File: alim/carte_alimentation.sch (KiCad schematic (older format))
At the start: 26 parts, among them J11 Conn_01x02_Male, J12 Conn_01x02_Male, J21 Conn_01x02_Male, J22 Conn_01x02_Male, J31 Conn_01x02_Male, J32 Conn_01x02_Male, J40 Conn_01x02_Male, J41 Conn_01x02_Male, J42 Conn_01x02_Male, J43 Conn_01x02_Male, U1 LM2576T-5, U2 LM2576T-5, U3 LM2576T-5

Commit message: ajout relais arret urgence
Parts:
- added K4: DIPxx-1Axx-11x, Relay_THT:Relay_StandexMeder_DIP_LowProfile, symbol Relay:DIPxx-1Axx-11x
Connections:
- wire segments 69 -> 72
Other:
- note added: "arret urgence NC\n"
- note removed: "arret urgence\n"
- moved on the sheet: C11, C12, C21, C22, D1, D2, J11, J12, J21, J22, J41, J42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

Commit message: Retrait relais, on fait passer toute la puissance par les arrêt d'urgence
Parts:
- removed K4: DIPxx-1Axx-11x, Relay_THT:Relay_StandexMeder_DIP_LowProfile, symbol Relay:DIPxx-1Axx-11x
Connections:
- wire segments 72 -> 69
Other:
- moved on the sheet: J42
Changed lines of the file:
@@
 	1    0    0    -1
 $EndComp
-Text Notes 3100 1200 0    50   ~ 0
+Text Notes 2950 1700 0    50   ~ 0
 arret urgence NC\n
 Wire Wire Line
@@
 	8200 3950 9050 3950
 $Comp
-L Relay:DIPxx-1Axx-11x K4
-U 1 1 5DE5847D
-P 2850 1800
-F 0 "K4" V 2283 1800 50  0000 C CNN
-F 1 "DIPxx-1Axx-11x" V 2374 1800 50  0000 C CNN
-F 2 "Relay_THT:Relay_StandexMeder_DIP_LowProfile" H 3200 1750 50  0001 L CNN
-F 3 "https://standexelectronics.com/wp-content/uploads/datasheet_reed_relay_DIP.pdf" H 2850 1800 50  0001 C CNN
-	1    2850 1800
-	0    1    1    0
-$EndComp
-Wire Wire Line
-	2550 2000 2450 2000
-$Comp
 L Connector:Conn_01x02_Male J42
 U 1 1 5DE1629E
-P 3250 1400
-F 0 "J42" V 3312 1444 50  0000 L CNN
-F 1 "Conn_01x02_Male" V 3403 1444 50  0000 L CNN
-F 2 "TerminalBlock:TerminalBlock_bornier-2_P5.08mm" H 3250 1400 50  0001 C CNN
-F 3 "~" H 3250 1400 50  0001 C CNN
-	1    3250 1400
+P 3150 1800
+F 0 "J42" V 3212 1844 50  0000 L CNN
+F 1 "Conn_01x02_Male" V 3303 1844 50  0000 L CNN
+F 2 "TerminalBlock:TerminalBlock_bornier-2_P5.08mm" H 3150 1800 50  0001 C CNN
+F 3 "~" H 3150 1800 50  0001 C CNN
+	1    3150 1800
 	0    1    1    0
 $EndComp
@@
 Wire Wire Line
 	4700 2000 3150 2000
-$Comp
-L power:GND #PWR0124
-U 1 1 5DE8EA76
-P 3250 1600
-F 0 "#PWR0124" H 3250 1350 50  0001 C CNN
-F 1 "GND" H 3255 1427 50  0000 C CNN
-F 2 "" H 3250 1600 50  0001 C CNN
-F 3 "" H 3250 1600 50  0001 C CNN
-	1    3250 1600
-	1    0    0    -1
-$EndComp
-Wire Wire Line
-	2550 1600 1950 1600
-Wire Wire Line
-	1950 1600 1950 2000
-Wire Wire Line
-	1900 2000 1950 2000
-Wire Wire Line
-	1950 2000 2150 2000
-Connection ~ 1950 2000
 Text Notes 4600 1150 0    50   ~ 0
 puissance moteurs\n
+Wire Wire Line
+	1900 2000 2150 2000
+Wire Wire Line
+	2450 2000 3050 2000
 $EndSCHEMATC

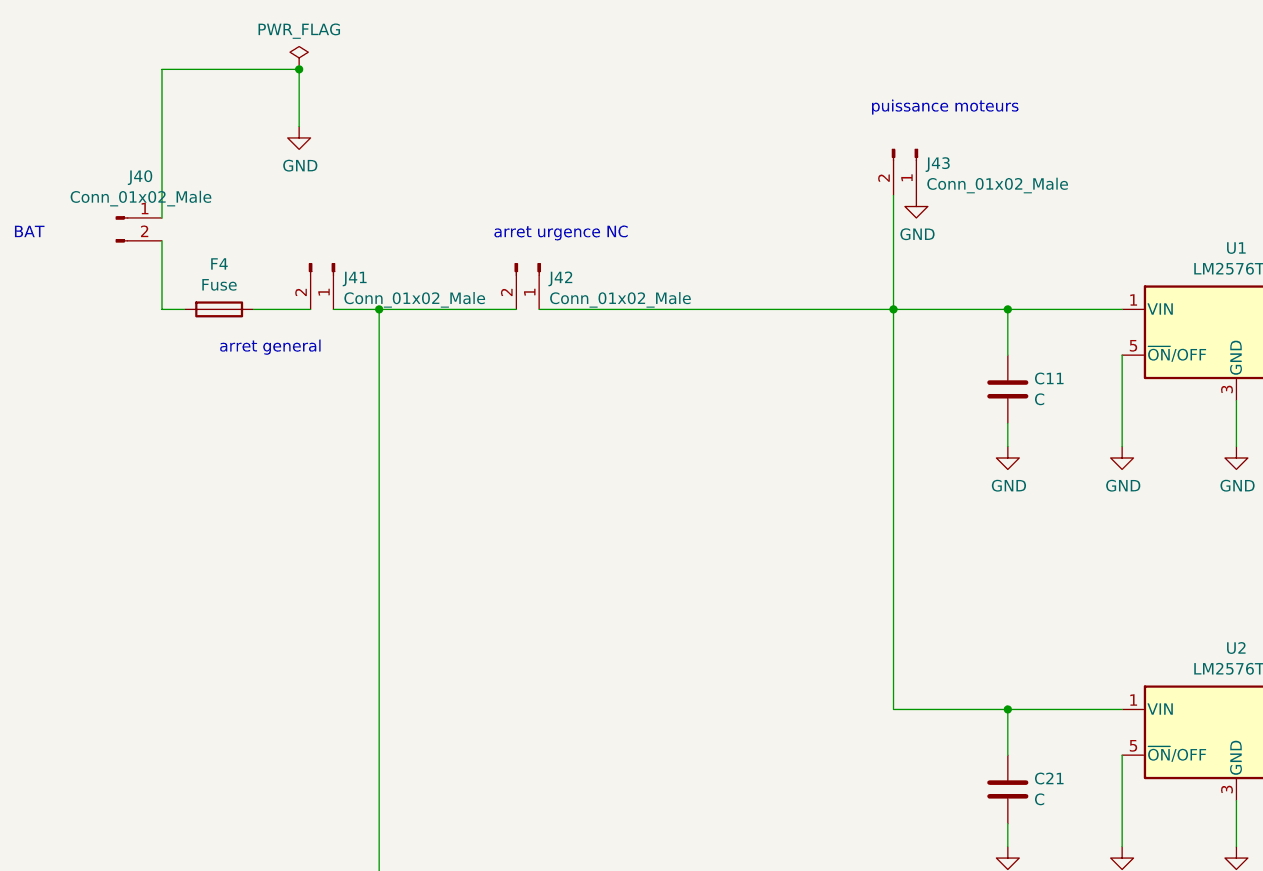
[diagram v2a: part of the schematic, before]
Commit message: ajout deuxieme fusible et empreinte
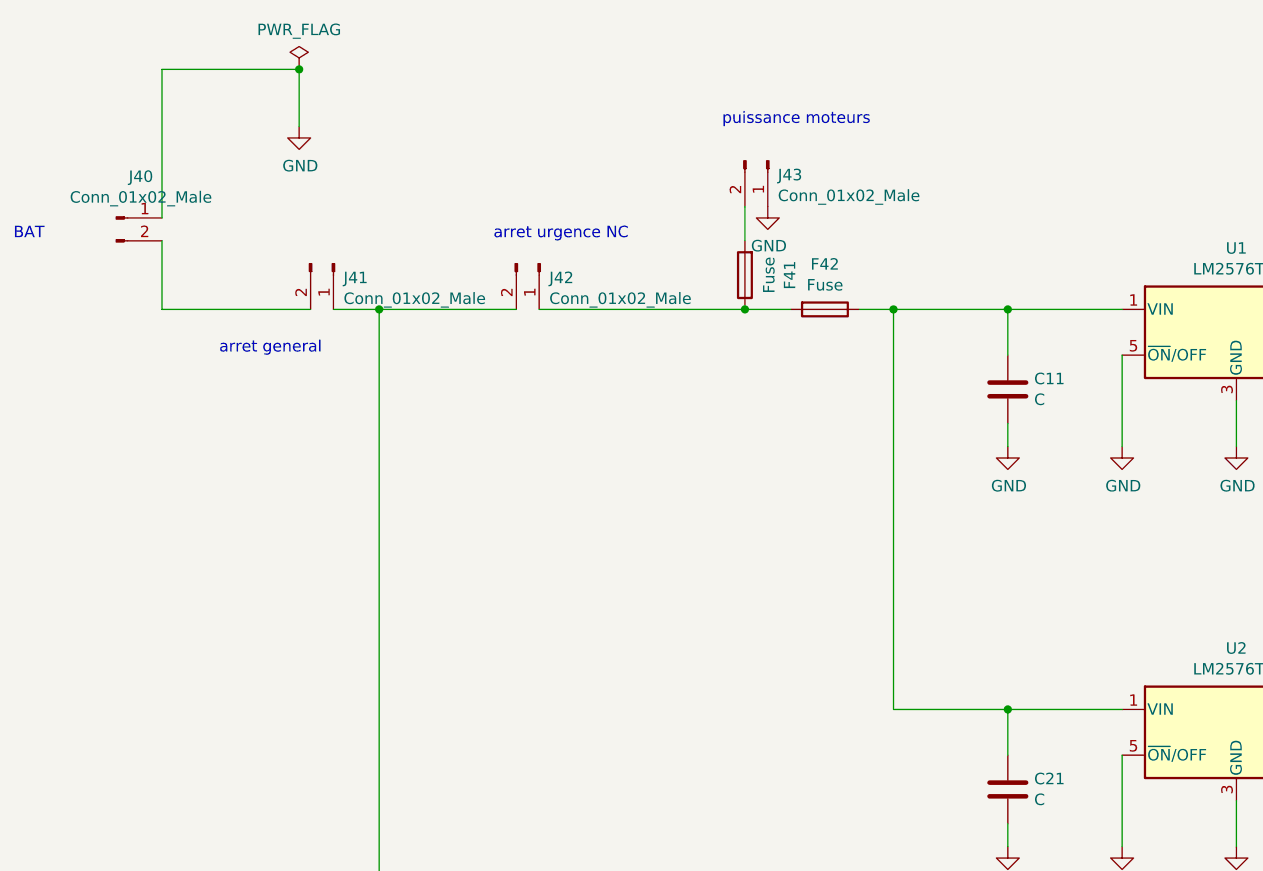
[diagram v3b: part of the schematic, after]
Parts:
- added F42: Fuse, symbol Device:Fuse
- C11, C12, C21, C22, C31, C32: footprint (none) -> Capacitor_THT:CP_Radial_D10.0mm_P5.00mm
- D1, D2, D3: footprint (none) -> Diode_THT:D_DO-27_P12.70mm_Horizontal
- renumbered F4 to F41
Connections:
- net at C11.1, C21.1, U1.1 (VIN)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: now also F42.1; no longer J42.1 (Pin_1), J43.2 (Pin_2)
- net at J40.2 (Pin_2): now also J41.2 (Pin_2); no longer F41.2
- net at F41.1: now also J42.1 (Pin_1), F42.2; no longer J41.2 (Pin_2)
- new net: F41.2, J43.2 (Pin_2)
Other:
- moved on the sheet: F41, J43
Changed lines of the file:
@@
 F 0 "C22" H 8085 4054 50  0000 R CNN
 F 1 "C" H 8085 4145 50  0000 R CNN
-F 2 "" H 8238 3950 50  0001 C CNN
+F 2 "Capacitor_THT:CP_Radial_D10.0mm_P5.00mm" H 8238 3950 50  0001 C CNN
 F 3 "~" H 8200 4100 50  0001 C CNN
 	1    8200 4100
@@
 F 0 "D2" V 7154 4179 50  0000 L CNN
 F 1 "D_Schottky" V 7245 4179 50  0000 L CNN
-F 2 "" H 7200 4100 50  0001 C CNN
+F 2 "Diode_THT:D_DO-27_P12.70mm_Horizontal" H 7200 4100 50  0001 C CNN
 F 3 "~" H 7200 4100 50  0001 C CNN
 	1    7200 4100
@@
 F 0 "C21" H 5315 4146 50  0000 L CNN
 F 1 "C" H 5315 4055 50  0000 L CNN
-F 2 "" H 5238 3950 50  0001 C CNN
+F 2 "Capacitor_THT:CP_Radial_D10.0mm_P5.00mm" H 5238 3950 50  0001 C CNN
 F 3 "~" H 5200 4100 50  0001 C CNN
 	1    5200 4100
@@
 F 0 "C12" H 8085 2304 50  0000 R CNN
 F 1 "C" H 8085 2395 50  0000 R CNN
-F 2 "" H 8238 2200 50  0001 C CNN
+F 2 "Capacitor_THT:CP_Radial_D10.0mm_P5.00mm" H 8238 2200 50  0001 C CNN
 F 3 "~" H 8200 2350 50  0001 C CNN
 	1    8200 2350
@@
 F 0 "D1" V 7154 2429 50  0000 L CNN
 F 1 "D_Schottky" V 7245 2429 50  0000 L CNN
-F 2 "" H 7200 2350 50  0001 C CNN
+F 2 "Diode_THT:D_DO-27_P12.70mm_Horizontal" H 7200 2350 50  0001 C CNN
 F 3 "~" H 7200 2350 50  0001 C CNN
 	1    7200 2350
@@
 F 0 "C11" H 5315 2396 50  0000 L CNN
 F 1 "C" H 5315 2305 50  0000 L CNN
-F 2 "" H 5238 2200 50  0001 C CNN
+F 2 "Capacitor_THT:CP_Radial_D10.0mm_P5.00mm" H 5238 2200 50  0001 C CNN
 F 3 "~" H 5200 2350 50  0001 C CNN
 	1    5200 2350
@@
 F 0 "C32" H 7385 5804 50  0000 R CNN
 F 1 "C" H 7385 5895 50  0000 R CNN
-F 2 "" H 7538 5700 50  0001 C CNN
+F 2 "Capacitor_THT:CP_Radial_D10.0mm_P5.00mm" H 7538 5700 50  0001 C CNN
 F 3 "~" H 7500 5850 50  0001 C CNN
 	1    7500 5850
@@
 F 0 "D3" V 6454 5929 50  0000 L CNN
 F 1 "D_Schottky" V 6545 5929 50  0000 L CNN
-F 2 "" H 6500 5850 50  0001 C CNN
+F 2 "Diode_THT:D_DO-27_P12.70mm_Horizontal" H 6500 5850 50  0001 C CNN
 F 3 "~" H 6500 5850 50  0001 C CNN
 	1    6500 5850
@@
 F 0 "C31" H 4615 5896 50  0000 L CNN
 F 1 "C" H 4615 5805 50  0000 L CNN
-F 2 "" H 4538 5700 50  0001 C CNN
+F 2 "Capacitor_THT:CP_Radial_D10.0mm_P5.00mm" H 4538 5700 50  0001 C CNN
 F 3 "~" H 4500 5850 50  0001 C CNN
 	1    4500 5850
@@
 arret urgence NC\n
 Wire Wire Line
-	4700 2000 4700 3750
-Connection ~ 4700 2000
-Wire Wire Line
-	4700 2000 5200 2000
-Wire Wire Line
 	1500 2000 1500 1700
 Wire Wire Line
@@
 L Connector:Conn_01x02_Male J43
 U 1 1 5DE73A34
-P 4800 1300
-F 0 "J43" V 4862 1344 50  0000 L CNN
-F 1 "Conn_01x02_Male" V 4953 1344 50  0000 L CNN
-F 2 "TerminalBlock:TerminalBlock_bornier-2_P5.08mm" H 4800 1300 50  0001 C CNN
-F 3 "~" H 4800 1300 50  0001 C CNN
-	1    4800 1300
-	0    1    1    0
-$EndComp
-Wire Wire Line
-	4700 2000 4700 1500
+P 4150 1350
+F 0 "J43" V 4212 1394 50  0000 L CNN
+F 1 "Conn_01x02_Male" V 4303 1394 50  0000 L CNN
+F 2 "TerminalBlock:TerminalBlock_bornier-2_P5.08mm" H 4150 1350 50  0001 C CNN
+F 3 "~" H 4150 1350 50  0001 C CNN
+	1    4150 1350
+	0    1    1    0
+$EndComp
 $Comp
 L power:GND #PWR0118
 U 1 1 5DE759C9
-P 4800 1500
-F 0 "#PWR0118" H 4800 1250 50  0001 C CNN
-F 1 "GND" H 4805 1327 50  0000 C CNN
-F 2 "" H 4800 1500 50  0001 C CNN
-F 3 "" H 4800 1500 50  0001 C CNN
-	1    4800 1500
-	1    0    0    -1
-$EndComp
-$Comp
-L Device:Fuse F4
+P 4150 1550
+F 0 "#PWR0118" H 4150 1300 50  0001 C CNN
+F 1 "GND" H 4155 1377 50  0000 C CNN
+F 2 "" H 4150 1550 50  0001 C CNN
+F 3 "" H 4150 1550 50  0001 C CNN
+	1    4150 1550
+	1    0    0    -1
+$EndComp
+$Comp
+L Device:Fuse F41
 U 1 1 5DE79EE7
-P 1750 2000
-F 0 "F4" V 1553 2000 50  0000 C CNN
-F 1 "Fuse" V 1644 2000 50  0000 C CNN
-F 2 "" V 1680 2000 50  0001 C CNN
-F 3 "~" H 1750 2000 50  0001 C CNN
-	1    1750 2000
-	0    1    1    0
-$EndComp
-Wire Wire Line
-	1600 2000 1500 2000
+P 4050 1850
+F 0 "F41" V 3853 1850 50  0000 C CNN
+F 1 "Fuse" V 3944 1850 50  0000 C CNN
+F 2 "" V 3980 1850 50  0001 C CNN
+F 3 "~" H 4050 1850 50  0001 C CNN
+	1    4050 1850
+	-1   0    0    1
+$EndComp
 $Comp
 L Connector:Conn_01x02_Male J21
@@
 	2250 2000 2450 2000
 Connection ~ 2450 2000
-Wire Wire Line
-	4700 2000 3150 2000
-Text Notes 4600 1150 0    50   ~ 0
+Text Notes 3950 1200 0    50   ~ 0
 puissance moteurs\n
 Wire Wire Line
-	1900 2000 2150 2000
-Wire Wire Line
 	2450 2000 3050 2000
+$Comp
+L Device:Fuse F42
+U 1 1 5DEE6FC7
+P 4400 2000
+F 0 "F42" V 4203 2000 50  0000 C CNN
+F 1 "Fuse" V 4294 2000 50  0000 C CNN
+F 2 "" V 4330 2000 50  0001 C CNN
+F 3 "~" H 4400 2000 50  0001 C CNN
+	1    4400 2000
+	0    1    1    0
+$EndComp
+Wire Wire Line
+	4050 1700 4050 1550
+Wire Wire Line
+	3150 2000 4050 2000
+Wire Wire Line
+	1500 2000 2150 2000
+Connection ~ 4050 2000
+Wire Wire Line
+	4050 2000 4250 2000
+Wire Wire Line
+	4550 2000 4700 2000
+Wire Wire Line
+	4700 3750 4700 2000
+Connection ~ 4700 2000
+Wire Wire Line
+	4700 2000 5200 2000
 $EndSCHEMATC
